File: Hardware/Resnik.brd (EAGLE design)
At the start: 53.3 x 100 mm, 99 parts, among them J2 CONN_82.54_SCREW, J3 CONN_42.54_SCREW, J4 CONN_82.54_SCREW, Q1 DMG3404, Q2 DMG3404, Q3 FDN360P, Q4 FDN360P, U1 TPS61030RSA, U10 MIC2039MT, U11 MIC2039MT, U12 SN74AUP2G08DQE, U13 SN74AUP1G04DCK, U14 MIC2039MT, U15 MIC2039MT, U16 SN74AUP2G08DQE, U17 SN74AUP1G04DCK, U18 TXS0102DQM, U19 LTC4412S6, U2 TPS62822DLC, U3 TLV61220DBV, U4 BQ2980RUG, U6 TPS22917DBV, U7 TPS22917DBV, U8 SN74AUP2G08DQE, U9 SN74AUP2G86SOT833-1

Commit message: Continued schematic additions, prelim part placement
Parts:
- removed R6: 180k, bschulz_passives:R0603
- removed R7: 820k, bschulz_passives:R0603
- removed U$18: TPS2105, bschulz:SOT23-5
- removed U$6: TPS79733, bschulz:DCK_R-PDSO-G5
- added C22, C24, C28, C29, C31, C32, C33, C34, C35, C36: 0.1uF, bschulz_passives:C0402
- added C23, C30: 10uF, bschulz_passives:C0805
- added C25: 1uF, bschulz_passives:C0402
- added C26, C27, CX2, CX3: 12pF, bschulz_passives:C0402
- added D+, D-: 27, bschulz_passives:R0402
- added D2, D3: (no value), bschulz:SOT23-3
- added D4, D5: (no value), bschulz:DO214AC
- added F1: PPTC1.5A, bschulz:1206
- added IC1: ATMEGA644M, bschulz:MLF44-TH
- added ISP2: AVRISP-6, bschulz:AVRISP
- added J5, J6, J7: (no value), bschulz:1X02_2.54_SCREWTERM
- added J8: (no value), bschulz:JST-2-SMD
- added JP5, JP6, JP7: JUMPER-SMT_2_NO_SILK, SparkFun-Jumpers:SMT-JUMPER_2_NO_SILK
- added MICRO_USB: MICRO_USB_LONGPADS, bschulz:10118194-0001LF_10118194-0001LF_LONGER_PADS
- added Q5: FDN360P, transistor-power:SUPER-SOT3
- added Q6: DMG3404, bschulz:SOT23-3
- added R35, R36, R37, R38, R39, R40, R41, R42: 330, bschulz_passives:R0402
- added R43, R44, R45, R48, R49: 10k, bschulz_passives:R0402
- added R46: 180k, bschulz_passives:R0402
- added R47: 120k, bschulz:R0603
- added R50: 330R, bschulz:R0603
- added R51: (no value), bschulz:R0603
- added R52, R53: 10k, bschulz_passives:R0603
- added U$1: CRYSTAL8MHZ5X3.2, bschulz:CRYSTAL_5X3.2_2-SMD
- added U$13: SN74LVC1G3157DRL, bschulz:DRL_R-PDSO-N6
- added U$15, U$16: CLVBA-FKA, bschulz:CLVBA-FKA
- added U$17: SN74AUP3G34DCU, bschulz:DCU_(R-PDSO-G8)
- added U$2: MICROSD, bschulz:MICROSD
- added U$3: TPL5111DDC, bschulz:DDC_R-PDSO-G6
- added U$5, U$9: BUTTON4.2X3.2, bschulz:SWITCH_4.2X3.2
- added U20, U24: TPS22917DBV, bschulz:DBV_R-PDSO-G6
- added U21: TXS0102DQM, bschulz:DQM_R-PX2SON-N8
- added U23: FT231X-Q, bschulz:QFN20
- added U25, U26: TXS0108RGY, bschulz:RGY_S-PVQFN-N20
- added U27: TXS0104RGY, bschulz:RGY_S-PVQFN-N14
- added U28: MCP4726A2SOT-23, bschulz:SOT23-6L
- added U29, U30: ADS1115, bschulz:VSSOP_10
- added U31: INA211DCK, bschulz:DCK_R-PDSO-G6
- added U32: INA210DCK, bschulz:DCK_R-PDSO-G6
- added U33: TCA9555RTW, bschulz:RTW_S-PWQFN-N24
- C1: value 22uF -> 4.7uF
- C10, C19, C20: value 0.1uF -> 22uF; device bschulz_passives:C0402 -> bschulz_passives:C0805
- C12, C15, C16: value 22uF -> 0.1uF; device bschulz_passives:C0805 -> bschulz_passives:C0402
- C13: value 10uF -> 1uF; device bschulz_passives:C0805 -> bschulz_passives:C0603
- C14: value 1uF -> 10uF; device bschulz_passives:C0603 -> bschulz_passives:C0805
- C18: value 0.1uF -> 1uF; device bschulz_passives:C0402 -> bschulz_passives:C0603
- C2: value 220uF -> 22uF; device bschulz_passives:C2917 -> bschulz_passives:C0805
- C21: value 1uF -> 0.1uF; device bschulz_passives:C0603 -> bschulz_passives:C0402
- C3: value 2.2uF -> 10uF
- C4: value 4.7uF -> 10uF
- C5: value 68pF -> 220uF; device bschulz_passives:C0402 -> bschulz_passives:C2917
- C6: value 22uF -> 68pF; device bschulz_passives:C0805 -> bschulz_passives:C0402
- C7: value 22uF -> 2.2uF
- C8, C9: value 10uF -> 22uF
- J1: value (none) -> CONN_82.54_SCREW; device bschulz:1X10_SCREW -> bschulz:1X08_SCREW
- J2: value CONN_82.54_SCREW -> (none); device bschulz:1X08_SCREW -> bschulz:1X10_SCREW
- J3: value CONN_42.54_SCREW -> CONN_82.54_SCREW; device bschulz:1X04_SCREW -> bschulz:1X08_SCREW
- J4: value CONN_82.54_SCREW -> CONN_42.54_SCREW; device bschulz:1X08_SCREW -> bschulz:1X04_SCREW
- L1: value 10uH -> 6.8uH; device bschulz:WE-XHMI(6.65X6.45) -> bschulz:1008
- L2: value 1uH -> 10uH; device bschulz:WE-LQS(3X3) -> bschulz:WE-XHMI(6.65X6.45)
- L3: value 6.8uH -> 1uH; device bschulz:1008 -> bschulz:WE-LQS(3X3)
- R1, R9: value 1.62M -> 180k
- R11: value 20R -> 330R
- R12: value 330R -> 3m; device bschulz:R0402 -> bschulz_passives:R0805
- R13: value (none) -> 20R
- R14: value 100R -> (none)
- R15: value 2k -> 91k
- R16: value 3m -> 100R; device bschulz_passives:R0805 -> bschulz:R0402
- R17: value 91k -> 2k
- R2: value 360k -> 1.62M
- R21: value 10k -> (none); device bschulz_passives:R0402 -> bschulz:R0603
- R22, R23, R24, R25: value 287R -> 10k; device bschulz_passives:R0603 -> bschulz_passives:R0402
- R27, R28, R29, R30: device bschulz_passives:R0603 -> bschulz_passives:R0402
- R3: value 1.62M -> 360k
- R31, R32, R33: value 10k -> 287R
- R34: value (none) -> 287R; device bschulz:R0603 -> bschulz_passives:R0402
- R4: value 180k -> 1.62M
- R8: value 180k -> 820k
- U1: value TPS61030RSA -> TLV61220DBV; device bschulz:RSA_S-PVQFN-N16 -> bschulz:DBV_R-PDSO-G6
- U10: value MIC2039MT -> SN74AUP1G04DCK; device bschulz:DFN_6_2X2 -> bschulz:DCK_R-PDSO-G5
- U11: value MIC2039MT -> SN74AUP2G86SOT833-1; device bschulz:DFN_6_2X2 -> bschulz:SOT833-1
- U13: value SN74AUP1G04DCK -> SN74AUP2G08DQE; device bschulz:DCK_R-PDSO-G5 -> bschulz:DQE_R-PX2SON-N8
- U14: value MIC2039MT -> SN74AUP2G08DQE; device bschulz:DFN_6_2X2 -> bschulz:DQE_R-PX2SON-N8
- U16: value SN74AUP2G08DQE -> MIC2039MT; device bschulz:DQE_R-PX2SON-N8 -> bschulz:DFN_6_2X2
- U17: value SN74AUP1G04DCK -> MIC2039MT; device bschulz:DCK_R-PDSO-G5 -> bschulz:DFN_6_2X2
- U18: value TXS0102DQM -> MIC2039MT; device bschulz:DQM_R-PX2SON-N8 -> bschulz:DFN_6_2X2
- U19: value LTC4412S6 -> TPS22917DBV; device bschulz:SOT23-6L -> bschulz:DBV_R-PDSO-G6
- U3: value TLV61220DBV -> TPS61032RSA; device bschulz:DBV_R-PDSO-G6 -> bschulz:RSA_S-PVQFN-N16
- U4: value BQ2980RUG -> (none); device bschulz:RUG_S-PQFP-N8 -> bschulz:DFN_12_3X3
- U5: value (none) -> BQ2980RUG; device bschulz:DFN_12_3X3 -> bschulz:RUG_S-PQFP-N8
- U6: value TPS22917DBV -> TPS2105; device bschulz:DBV_R-PDSO-G6 -> bschulz:SOT23-5
- U7: value TPS22917DBV -> LTC4412S6; device bschulz:DBV_R-PDSO-G6 -> bschulz:SOT23-6L
- U8: value SN74AUP2G08DQE -> TPS79733; device bschulz:DQE_R-PX2SON-N8 -> bschulz:DCK_R-PDSO-G5
- U9: value SN74AUP2G86SOT833-1 -> SN74AUP1G04DCK; device bschulz:SOT833-1 -> bschulz:DCK_R-PDSO-G5
- moved RTC1 279.4 mm to (48.3, 71.1)
- moved R34 277.5 mm to (8.89, 54.1), turned to 270 degrees
- moved R33 269.2 mm to (11.4, 59.7)
- moved C20 264.2 mm to (10.2, 52.1)
- moved C19 262.6 mm to (44.5, 39.4), turned to 180 degrees
- moved BT1 258.0 mm to (47.0, 57.1), turned to 90 degrees
- moved Q4 251.3 mm to (24.4, 14.7), turned to 180 degrees
- moved C18 250.4 mm to (39.4, 23.9), turned to 180 degrees
- moved Q3 249.5 mm to (27.6, 14.7), turned to 180 degrees
- moved U19 249.0 mm to (28.1, 18.8)
- moved R32 248.0 mm to (44.6, 47.0)
- moved R31 237.6 mm to (44.6, 43.2), turned to 180 degrees
- moved U18 233.1 mm to (11.4, 54.6), turned to 270 degrees
- moved S1 233.0 mm to (39.0, 50.3), turned to 180 degrees
- moved C17 229.9 mm to (39.5, 18.9), turned to 180 degrees
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- renumbered U$12 to U22
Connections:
- removed net N$1: R3.1, R4.2, U1.14
- removed net N$17: U6.5, U6.6
- removed net N$19: U7.5, U7.6
- removed net N$42: R32.2, S2.2
- new net 3V3: C25.1, IC1.17, IC1.27, IC1.29, IC1.38, IC1.5, ISP2.2, R44.2, U$16.2
- new net 3V3_AUX_CTRL: IC1.25
- new net 3V3_FTDI: C24.1, U23.10, U23.11, U23.20
- new net ADC_0: JP7.1, U30.4
- new net ADC_1: U30.5
- new net ADC_2: U30.6
- new net ADC_3: JP6.1, U30.7
- new net ADC_EXT: IC1.37
- new net ADC_EXT_ALERT: U30.2
- new net ADC_OB_ALERT: U29.2
- new net ALIVE_LED: IC1.23, R39.2
- new net BAT_SENSE: IC1.35
- new net BUS_LOGIC_EN_PRIME: R48.1, U25.10, U27.8
- new net BUS_LOGIC_EN_SEC: R49.1, U26.10
- new net CS_EXT: U27.5
- new net CS_OUT: U27.10
- new net DAC_OUT: C31.1, U28.1
- new net DTR: C28.1, U23.18
- new net EN_BUS_SEC: R25.1, U12.1, U12.6
- new net FEATHER_BAT: U24.5, U24.6
- new net FEATHER_EN: Q5.1, R46.1
- new net GPIO_0: U25.4
- new net GPIO_0_OUT: U25.17
- new net GPIO_1: U25.5
- new net GPIO_1_OUT: U25.16
- new net GPIO_2: U26.4
- new net GPIO_2_OUT: U26.17
- new net GPIO_3: U26.5
- new net GPIO_3_OUT: U26.16
- new net GPIO_EXT: IC1.43
- new net I_LI: U29.6, U31.6
- new net I_SOLAR: U29.4, U32.6
- new net LED1: IC1.14, R42.1
- new net LED2: IC1.15, R40.1
- new net LED3: IC1.16, R41.1
- new net LOG_INT: IC1.33, R43.1, U$5.3, U$5.4
- new net MISO: IC1.2, ISP2.1, U$2.7, U27.2
- new net MISO_OUT: U27.13
- new net MOSI: IC1.1, ISP2.4, U$17.3, U27.3
- new net MOSI_BUF: U$17.5, U$2.3
- new net MOSI_OUT: U27.12
- new net N$44: R38.2, U23.17
- new net N$47: R37.2, U23.1
- new net N$48: CX3.2, D+.2, MICRO_USB.3
- new net N$49: CX2.2, D-.2, MICRO_USB.2
- new net N$50: D+.1, U23.8
- new net N$51: R36.2, U23.14
- new net N$52: D-.1, U23.9
- new net N$53: R36.1, U$16.1
- new net N$54: R35.1, U$16.3
- new net N$56: R39.1, U$16.4
- new net N$57: R35.2, U23.7
- new net N$58: R40.2, U$15.3
- new net N$59: R41.2, U$15.4
- new net N$60: R42.2, U$15.1
- new net N$61: C27.2, IC1.7, U$1.OSC2
- new net N$62: C26.2, IC1.8, U$1.OSC1
- new net N$63: Q5.3, R47.2, U$3.3
- new net N$64: U$3.5, U24.3
- new net N$65: JP7.2, R53.2
- new net N$66: JP6.2, R52.2
- new net N$67: C10.1, D5.C, U4.1, U4.2
- new net PG: IC1.21
- new net RST: C28.2, IC1.4, ISP2.5, R44.1, U$9.3, U$9.4
- new net RX: IC1.9, R38.1
- new net RX_EXT: IC1.11, U25.7, U26.7
- new net RX_OUT_PRIME: U25.14
- new net RX_OUT_SEC: U26.14
- new net SCK: IC1.3, ISP2.3, U$17.1, U27.4
- new net SCK_BUF: U$17.7, U$2.5
- new net SCK_OUT: U27.11
- new net SCL_OUT_PRIME: U25.18
- new net SCL_OUT_SEC: U26.18
- new net SDA_CTRL: IC1.24, U$13.6
- new net SDA_EXT: JP5.2, U$13.1, U25.1, U26.1
- new net SDA_OUT_PRIME: U25.20
- new net SDA_OUT_SEC: U26.20
- new net SD_CD: IC1.41, R45.1, U$2.CD1
- new net SD_CS: IC1.44, U$17.6
- new net SD_CS_BUF: U$17.2, U$2.2
- new net SOLAR_SENSE+: L4.P$2, R20.1, U32.4, U4.10
- new net THERM_SENSE: IC1.36
- new net TX: IC1.10, R37.1
- new net TX_EXT: IC1.12, U25.6, U26.6
- new net TX_OUT_PRIME: U25.15
- new net TX_OUT_SEC: U26.15
- new net VBAT_SW_CTRL: IC1.22
- new net VBUS_SEC: C19.1, U15.1, U16.1, U26.19
- new net VCC: U33.21
- new net VREF: C32.1, D2.1, IC1.34, R50.1, U28.6
- new net VSWITCH_CTRL: IC1.13
- new net VUSB_POWER: F1.2, Q4.3
- new net V_PRIME-: J5.P1, Q6.3
- new net WD_DONE: U$3.4
- net 3V3_AUX: now also C21.1, C8.1, C9.1, L3.P$2, R25.2, R45.2, R48.2, R49.2, R8.2, U$13.5, U$17.8, U$2.4, U10.5, U13.8, U16.6, U18.6, U21.1, U21.5, U25.2, U26.2, U27.1, U9.5; no longer C17.1, C5.1, C7.1, L2.P$2, R21.2, R7.2, U10.6, U13.5, U14.6, U16.8, U17.5, U18.1, U18.5
- net 3V3_AUX_PG: now also R1.1; no longer R6.1
- net 3V3_CORE: now also C18.1, Q5.2, R22.2, R43.2, R46.2, U$15.2, U$3.1, U$3.6, U11.8, U14.8, U8.5; no longer C21.1, R33.2, U$6.5, U8.8, U9.8
- net 5V_AUX: now also C1.1, C29.1, C30.1, C33.1, C34.1, C35.1, C36.1, C5.+, C7.1, R1.2, R10.2, R50.2, R51.2, U17.6, U21.8, U28.3, U29.8, U3.1, U3.15, U3.16, U30.1, U30.8, U31.3, U32.3; no longer C2.+, C3.1, C4.1, R3.2, R5.2, R6.2, U1.1, U1.15, U1.16, U11.6, U18.8
- net 5V_LP: now also C15.1, C4.1, R4.2, U1.5, U6.1, U6.5; no longer C18.1, C9.1, R9.2, U$18.1, U$18.5, U3.5
- net BMS_CTR: now also R16.1; no longer R14.1
- net C0: now also U11.1, U11.6, U14.2; no longer U8.2, U9.1, U9.6
- net C1: now also U11.2, U11.5, U14.6; no longer U8.6, U9.2, U9.5
- net EN_BUS_PRIME: now also U13.1, U13.6; no longer R21.1, U12.1, U12.6, U16.1, U16.6
- net FAULT_PRIME: now also U16.3, U17.3, U18.3; no longer U10.3, U11.3, U14.3
- net GND: now also C14.2, C2.2, C22.2, C23.2, C24.2, C25.2, C26.1, C27.1, C29.2, C30.2, C31.2, C32.2, C33.2, C34.2, C35.2, C36.2, C5.-, CX2.1, CX3.1, D2.2, D3.2, D4.A, IC1.18, IC1.28, IC1.39, IC1.6, IC1.TH, ISP2.6, J7.P1, MICRO_USB.5, Q6.2, R12.2, R14.1, R23.1, R24.1, R28.2, R29.1, R3.1, R30.2, R47.1, R5.1, R52.1, R53.1, R9.1, U$13.2, U$17.4, U$2.6, U$2.CD2, U$2.MT1, U$2.MT2, U$3.2, U$5.1, U$5.2, U$9.1, U$9.2, U1.2, U10.3, U11.4, U13.4, U14.4, U16.5, U16.PAD, U16.PAD@1, U17.5, U17.PAD, U17.PAD@1, U18.5, U18.PAD, U18.PAD@1, U20.2, U21.4, U23.13, U23.3, U23.6, U23.EP, U24.2, U25.11, U25.EP, U26.11, U26.EP, U27.7, U27.EP, U28.2, U29.1, U29.3, U3.10, U3.13, U3.5, U3.6, U3.7, U3.PAD, U3.PAD@1, U3.PAD@2, U3.PAD@3, U3.PAD@4, U3.PAD@5, U3.PAD@6, U3.PAD@7, U3.PAD@8, U3.PAD@9, U30.3, U31.2, U31.4, U32.1, U32.2, U33.9, U33.EP, U4.6, U4.EP, U5.4, U8.2, U9.3; no longer C13.2, C2.-, C6.2, R10.1, R13.1, R16.2, R2.1, R22.1, R24.2, R29.2, R31.1, R32.1, R4.1, R8.1, U$18.2, U$6.2, U1.10, U1.13, U1.5, U1.6, U1.7, U1.PAD, U1.PAD@1, U1.PAD@2, U1.PAD@3, U1.PAD@4, U1.PAD@5, U1.PAD@6, U1.PAD@7, U1.PAD@8, U1.PAD@9, U10.5, U10.PAD, U10.PAD@1, U11.5, U11.PAD, U11.PAD@1, U13.3, U14.5, U14.PAD, U14.PAD@1, U16.4, U17.3, U18.4, U3.2, U4.4, U5.6, U5.EP, U8.4, U9.4
- net LBI: now also R10.1, U3.12; no longer R5.1, U1.12
- net LI+: now also J6.P2, J8.2, R13.2, U29.5; no longer R12.2
- net LI-: now also J6.P1, J8.1, R12.1, U31.5, U5.3; no longer R16.1, U4.3
- net MPPT_CHRG: now also U4.4; no longer U5.4
- net MPPT_FAULT: now also U4.5; no longer U5.5
- net MPPT_SHDN: now also U4.3; no longer U5.3
- net N$10: now also U5.7; no longer U4.7
- net N$11: now also R17.2, U5.6; no longer R15.2, U4.6
- net N$12: now also R15.1; no longer R17.1
- net N$13: now also C12.1, R16.2, U5.5; no longer C10.1, R13.2, U4.5
- net N$14: now also R13.1, U5.1; no longer R11.1, U4.1
- net N$15: now also R15.2, U4.7; no longer R17.2, U5.7
- net N$16: now also R11.1, U5.2; no longer R12.1, U4.2
- net N$18: now also C13.2, U4.11; no longer C14.2, U5.11
- net N$2: now also L3.P$1; no longer L2.P$1
- net N$20: now also C13.1, D4.C, U4.12; no longer C14.1, U5.12
- net N$21: now also D3.1, R51.1, U31.1; no longer L4.P$2, R20.1, U5.10
- net N$22: now also U11.7, U14.1; no longer U8.1, U9.7
- net N$23: now also U14.7, U19.3; no longer U7.3, U8.7
- net N$24: now also U14.3, U20.3; no longer U6.3, U8.3
- net N$25: now also U11.3, U14.5; no longer U8.5, U9.3
- net N$26: now also U10.4, U13.5; no longer U12.5, U13.4
- net N$27: now also R29.2, R33.2, U17.2; no longer R22.2, R23.2, U11.2
- net N$28: now also R24.2, S2.2, U10.2; no longer R31.2, S1.2, U12.2
- net N$29: now also U13.7, U17.4; no longer U11.4, U12.7
- net N$3: now also C6.2, R8.1, R9.2; no longer C5.2, R7.1, R8.2
- net N$30: now also U13.3, U18.4; no longer U10.4, U12.3
- net N$31: now also JP3.2, R33.1; no longer JP1.2, R23.1
- net N$32: now also JP4.2, R34.2; no longer JP2.2, R25.2
- net N$33: now also R30.1, R34.1, U18.2; no longer R24.1, R25.1, U10.2
- net N$34: now also U12.5, U9.4; no longer U16.5, U17.4
- net N$35: now also R23.2, S1.2, U12.2, U9.2; no longer U16.2, U17.2
- net N$36: now also U12.7; no longer U16.7
- net N$37: now also U12.3, U16.4; no longer U14.4, U16.3
- net N$38: now also R31.2; no longer R28.2
- net N$39: now also JP1.2, R31.1; no longer JP3.2, R28.1
- net N$4: now also R2.1, R3.2, U3.9; no longer R1.1, R2.2, U1.9
- net N$40: now also JP2.2, R32.2; no longer JP4.2, R30.2
- net N$41: now also R28.1, R32.1, U16.2; no longer R29.1, R30.1, U14.2
- net N$45: now also Q4.1, U7.5; no longer Q3.1, U19.5
- net N$46: now also Q3.1, R21.1, U7.4; no longer Q4.1, R34.1, U19.4
- net N$5: now also L2.2, U3.3, U3.4; no longer L1.2, U1.3, U1.4
- net N$7: now also R4.1, R5.2, U1.4; no longer R10.2, R9.1, U3.4
- net N$8: now also U5.8; no longer U4.8
- net N$9: now also L1.2, U1.1; no longer L3.2, U3.1
- net PG_LDO: now also R22.1, U8.1; no longer R33.1, U$6.1
- net RTC_INT: now also IC1.42
- net SCL: now also IC1.19, U21.3, U25.3, U26.3; no longer U18.3
- net SCL_5V: now also U21.6, U28.5, U29.10, U30.10; no longer U18.6
- net SDA: now also IC1.20, U$13.4, U21.2; no longer U18.2
- net SDA_5V: now also U21.7, U28.4, U29.9, U30.9; no longer U18.7
- net SDA_OB: now also JP5.1, U$13.3
- net VBAT+: now also C17.1, U6.4, U8.4; no longer C20.1, U$18.4, U$6.4
- net VBUS_PRIME: now also C20.1, U17.1, U18.1, U25.19, U27.14; no longer C15.1, C16.1, U10.1, U11.1, U14.1, U15.1
- net VUSB: now also C22.1, C23.1, F1.1, MICRO_USB.1, U23.12; no longer Q3.3
- net V_BETA: now also C3.1, L1.1, R21.2, U1.3, U1.6, U20.1, U7.6; no longer C8.1, L3.1, R34.2, U19.6, U3.3, U3.6, U6.1
- net V_BETA_CTL: now also U7.3; no longer U19.3
- net V_HP: now also C2.1, L2.1, R2.2, U19.5, U19.6, U20.5, U20.6, U3.11, U3.8; no longer C1.1, L1.1, R1.2, U1.11, U1.8
- net V_LI: now also C14.1, Q3.3, R17.1, U24.1, U32.5, U4.9, U7.1; no longer C13.1, Q4.3, R15.1, U19.1, U5.9
- net V_PRIME: now also C16.1, J5.P2, Q6.1, U19.1, U29.7, U6.3; no longer C19.1, U$18.3, U7.1
- net V_SOLAR: now also D5.A, J7.P2; no longer C12.1, U5.1, U5.2

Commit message: Preliminary power section layout
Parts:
- moved C21 276.8 mm to (52.1, 71.1), turned to 90 degrees
- moved U22 274.6 mm to (26.7, 73.7)
- moved C36 257.8 mm to (26.7, 52.1)
- moved U21 250.9 mm to (33.0, 59.7)
- moved U30 250.2 mm to (26.7, 49.5), turned to 270 degrees
- moved JP6 247.7 mm to (45.7, 29.2), flipped to the bottom, turned to 90 degrees
- moved JP7 244.2 mm to (6.35, 39.4), flipped to the bottom, turned to 270 degrees
- moved R52 242.5 mm to (44.5, 27.9), turned to 90 degrees
- moved R53 241.4 mm to (8.89, 39.4), turned to 90 degrees
- moved R23 238.9 mm to (38.1, 40.6)
- moved R24 224.1 mm to (14.0, 54.6)
- moved R45 195.7 mm to (2.54, 77.5)
- moved R49 193.7 mm to (40.5, 35.7)
- moved R48 191.5 mm to (10.0, 47.6)
- moved JP5 189.4 mm to (31.8, 64.8)
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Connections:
- removed net 3V3_AUX_CTRL: IC1.25
- removed net ADC_EXT: IC1.37
- removed net BAT_SENSE: IC1.35
- removed net GPIO_EXT: IC1.43
- removed net PG: IC1.21
- removed net THERM_SENSE: IC1.36
- removed net VBAT_SW_CTRL: IC1.22
- removed net VCC: U33.21
- removed net VSWITCH_CTRL: IC1.13
- new net FEATHER_CTS: IC1.31, MS1.20
- new net FEATHER_GPIO: IC1.32, MS1.10
- new net FEATHER_RTS: IC1.30, MS1.19
- new net GLOBAL_INT: IC1.34, U33.22
- net 3V3_CORE: now also U33.21
- net 5V_AUX: now also MS1.26
- net ADC_0: now also J2.1
- net ADC_1: now also J1.8
- net ADC_2: now also J3.5
- net ADC_3: now also J3.6
- net C0: now also IC1.21
- net C1: now also IC1.22
- net CS_OUT: now also J2.6
- net DAC_OUT: now also J1.7
- net EN_BUS_PRIME: now also IC1.25
- net EN_BUS_SEC: now also IC1.26
- net FEATHER_BAT: now also MS1.28
- net GND: now also J1.2, J2.10, J3.1, J4.2, U33.18, U33.23, U33.24
- net GPIO_0: now also IC1.13
- net GPIO_0_OUT: now also J1.6
- net GPIO_1_OUT: now also J1.5
- net GPIO_2: now also IC1.43, U26.5; no longer U26.4
- net GPIO_2_OUT: now also J3.7, U26.16; no longer U26.17
- net GPIO_3: now also U26.4; no longer U26.5
- net GPIO_3_OUT: now also J3.8, U26.17; no longer U26.16
- net MISO: now also MS1.13
- net MISO_OUT: now also J2.5
- net MOSI_BUF: now also MS1.12
- net MOSI_OUT: now also J2.4
- net RST: now also MS1.21
- net RX: now also MS1.15
- net RX_EXT: now also U26.1; no longer U26.7
- net RX_OUT_PRIME: now also J1.3
- net RX_OUT_SEC: now also J4.3, U26.20; no longer U26.14
- net SCK_BUF: now also MS1.11
- net SCK_OUT: now also J2.3
- net SCL: now also MS1.18, U26.6, U33.19; no longer U26.3
- net SCL_OUT_PRIME: now also J2.7
- net SCL_OUT_SEC: now also J3.4, U26.15; no longer U26.18
- net SDA_EXT: now also U26.7; no longer U26.1
- net SDA_OB: now also MS1.17, U33.20
- net SDA_OUT_PRIME: now also J2.8
- net SDA_OUT_SEC: now also J3.3, U26.14; no longer U26.20
- net TX: now also MS1.14
- net TX_EXT: now also U26.3; no longer U26.6
- net TX_OUT_PRIME: now also J1.4
- net TX_OUT_SEC: now also J4.4, U26.18; no longer U26.15
- net VBUS_PRIME: now also J1.1, J2.9
- net VBUS_SEC: now also J3.2, J4.1
- net VREF: now also J2.2; no longer IC1.34
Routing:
- net GND: track 0.00 -> 112.1 mm, vias 0 -> 1
- net V_LI: track 0.00 -> 35.8 mm
- net VUSB: track 0.00 -> 25.5 mm, vias 0 -> 2
- net VUSB_POWER: track 0.00 -> 24.6 mm, vias 0 -> 2
- net LI-: track 0.00 -> 21.1 mm
- net SOLAR_SENSE+: track 0.00 -> 18.6 mm
- net LI+: track 0.00 -> 18.3 mm
- net N$20: track 0.00 -> 12.4 mm
- net N$57: track 0.00 -> 12.2 mm, vias 0 -> 2
- net N$67: track 0.00 -> 11.9 mm
- net 3V3_FTDI: track 0.00 -> 9.36 mm, vias 0 -> 2
- net N$10: track 0.00 -> 8.42 mm
- net N$48: track 0.00 -> 8.40 mm
- net N$8: track 0.00 -> 8.08 mm
- net N$49: track 0.00 -> 7.70 mm
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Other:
- board text added: "3v3"
- board text added: "5v"

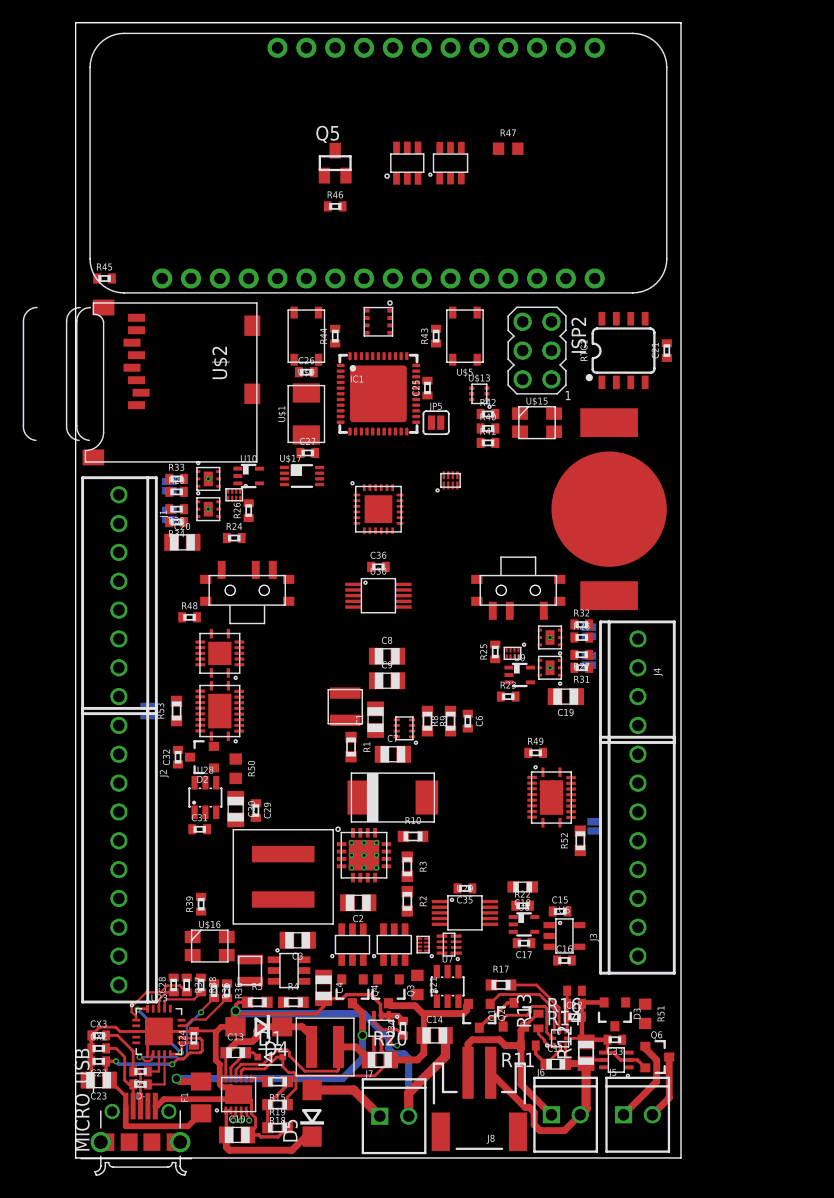
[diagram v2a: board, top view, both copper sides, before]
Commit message: Continued layout, board size change
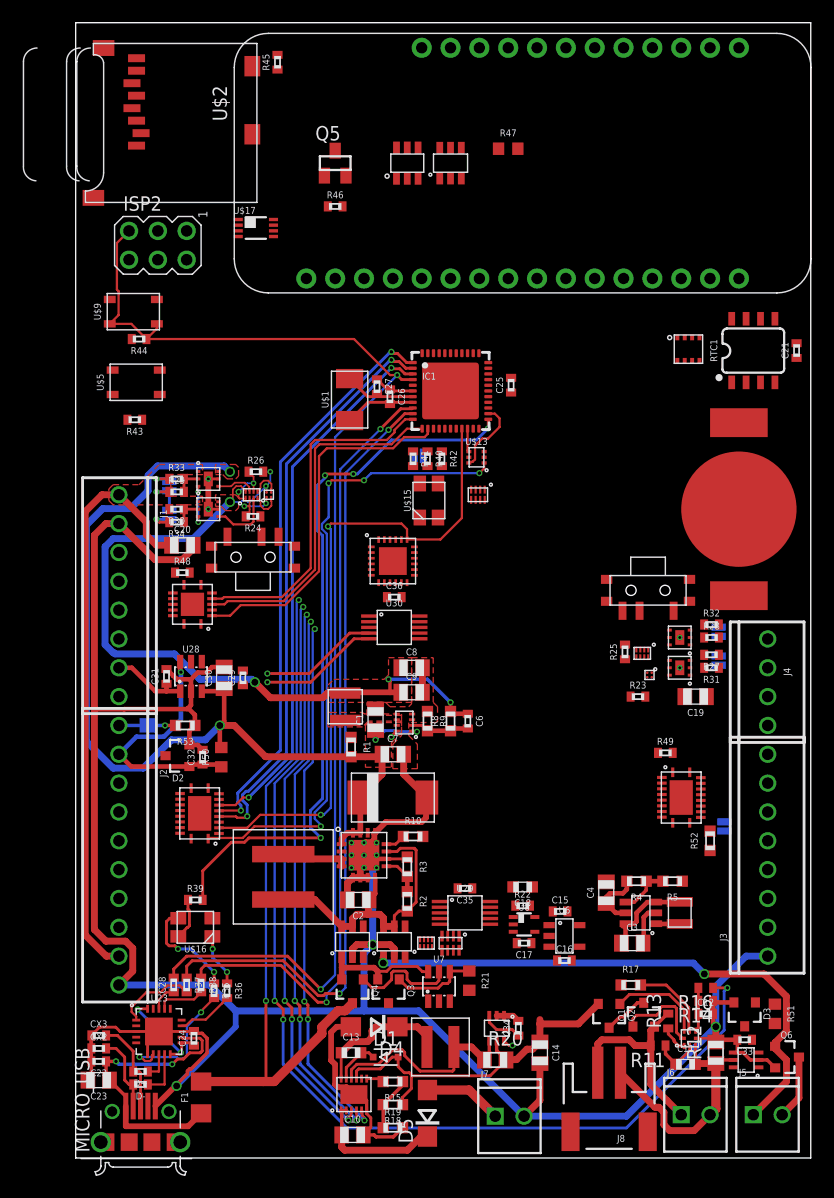
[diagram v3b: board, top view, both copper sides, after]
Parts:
- U10, U9: value SN74AUP1G04DCK -> SN74AUP1G04YFP; device bschulz:DCK_R-PDSO-G5 -> bschulz:DSBGD_4
- moved L1 38.2 mm to (53.2, 21.6), turned to 270 degrees
- moved R5 38.1 mm to (52.6, 24.4), turned to 180 degrees
- moved ISP2 34.7 mm to (7.24, 80.4), turned to 270 degrees
- moved R4 32.1 mm to (49.4, 24.4), turned to 180 degrees
- moved U1 31.4 mm to (49.8, 21.6), turned to 90 degrees
- moved C3 29.5 mm to (49.0, 18.9), turned to 0 degrees
- moved U$5 29.2 mm to (5.33, 68.3), turned to 0 degrees
- moved R43 27.5 mm to (5.21, 65.0), turned to 180 degrees
- moved U22 27.4 mm to (54.0, 71.2), turned to 90 degrees
- moved C4 26.3 mm to (46.7, 23.4), turned to 90 degrees
- moved R45 24.4 mm to (17.8, 96.5), turned to 90 degrees
- moved U$2 22.9 mm to (16.0, 98.2)
- moved U$17 22.2 mm to (15.9, 81.9)
- moved R44 17.3 mm to (5.59, 72.1), turned to 180 degrees
- moved U$9 15.4 mm to (5.08, 74.5), turned to 0 degrees
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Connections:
- net 3V3_AUX: now also U10.A2, U9.A2; no longer U10.5, U9.5
- net CS_EXT: now also U25.4; no longer U27.5
- net CS_OUT: now also U25.17; no longer U27.10
- net GND: now also U10.B1, U9.B1; no longer U10.3, U9.3
- net GPIO_0: now also U27.2; no longer U25.4
- net GPIO_0_OUT: now also U27.13; no longer U25.17
- net GPIO_1: now also U27.3; no longer U25.5
- net GPIO_1_OUT: now also U27.12; no longer U25.16
- net MISO: now also U25.5; no longer U27.2
- net MISO_OUT: now also U25.16; no longer U27.13
- net MOSI: now also U25.6; no longer U27.3
- net MOSI_OUT: now also U25.15; no longer U27.12
- net N$26: now also U10.B2; no longer U10.4
- net N$28: now also U10.A1; no longer U10.2
- net N$34: now also U9.B2; no longer U9.4
- net N$35: now also U9.A1; no longer U9.2
- net RX_EXT: now also U27.5; no longer U25.7
- net RX_OUT_PRIME: now also U27.10; no longer U25.14
- net SCK: now also U25.7; no longer U27.4
- net SCK_OUT: now also U25.14; no longer U27.11
- net TX_EXT: now also U27.4; no longer U25.6
- net TX_OUT_PRIME: now also U27.11; no longer U25.15
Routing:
- net GND: track 112.1 -> 287.5 mm, vias 1 -> 4
- net RST: track 0.00 -> 111.7 mm, vias 0 -> 2
- net BMS_CTR: track 0.00 -> 91.5 mm, vias 0 -> 4
- net 5V_AUX: track 3.62 -> 91.8 mm, vias 0 -> 4
- net TX: track 0.00 -> 70.2 mm, vias 0 -> 2
- net RX: track 0.00 -> 69.4 mm, vias 0 -> 2
- net 3V3_AUX: track 0.00 -> 68.5 mm, vias 0 -> 6
- net ALIVE_LED: track 0.00 -> 64.2 mm, vias 0 -> 4
- net SCL: track 0.00 -> 57.1 mm, vias 0 -> 2
- net SDA_EXT: track 0.00 -> 56.4 mm, vias 0 -> 4
- net VBUS_PRIME: track 0.00 -> 51.8 mm
- net MISO: track 0.00 -> 50.8 mm, vias 0 -> 2
- net MOSI: track 0.00 -> 50.4 mm, vias 0 -> 2
- net SCK: track 0.00 -> 48.0 mm, vias 0 -> 2
- net MPPT_SHDN: track 0.99 -> 48.7 mm, vias 1 -> 4
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- added copper zone on layer 1, net 3V3_AUX
- added copper zone on layer 1, net 5V_AUX
- added copper zone on layer 1, net GND
- added copper zone on layer 1, net N$2
- added copper zone on layer 1, net VBUS_PRIME
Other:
- board size 53.3 x 100 mm -> 64.8 x 100 mm
